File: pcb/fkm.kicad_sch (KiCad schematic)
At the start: 12 parts, among them U2 18650, U3 AMS1117-3.3

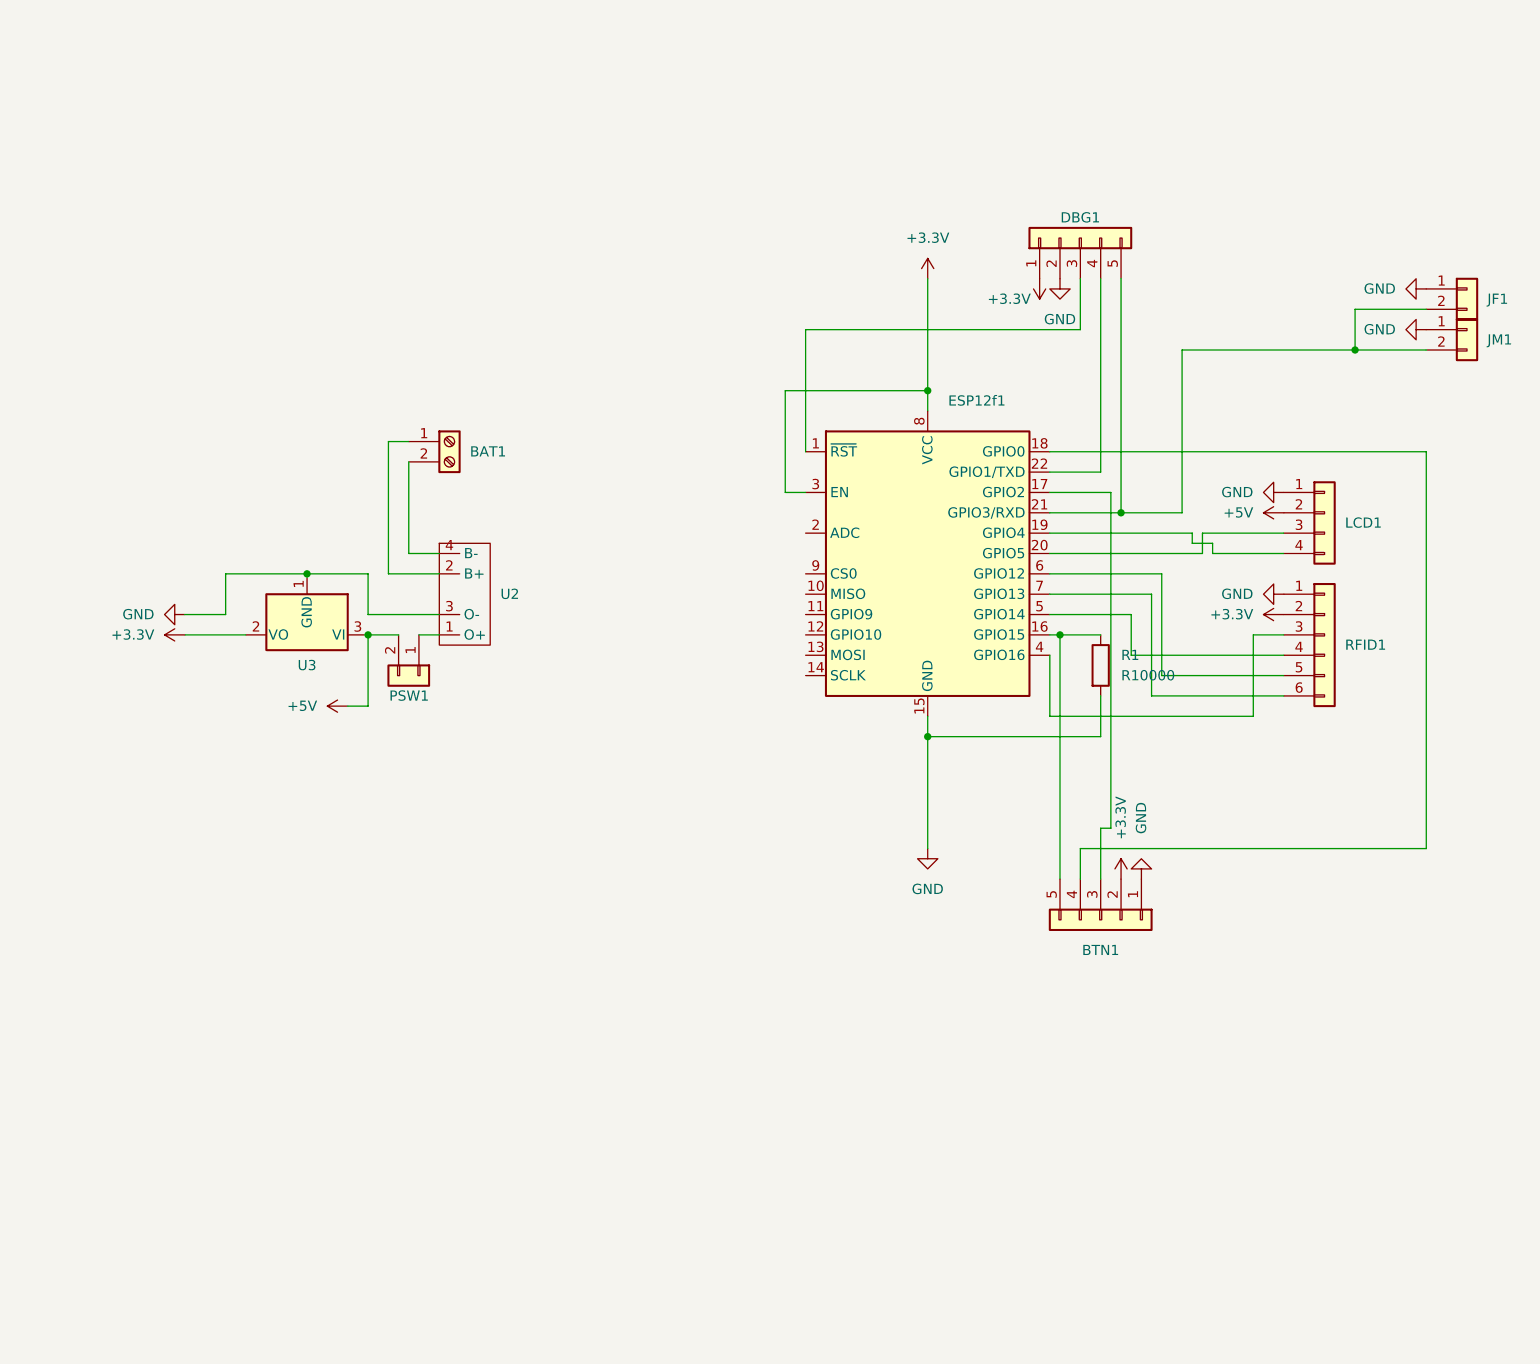
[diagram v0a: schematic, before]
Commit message: wip(pcb): rev 2.0 pcb (esp32) - to re-do
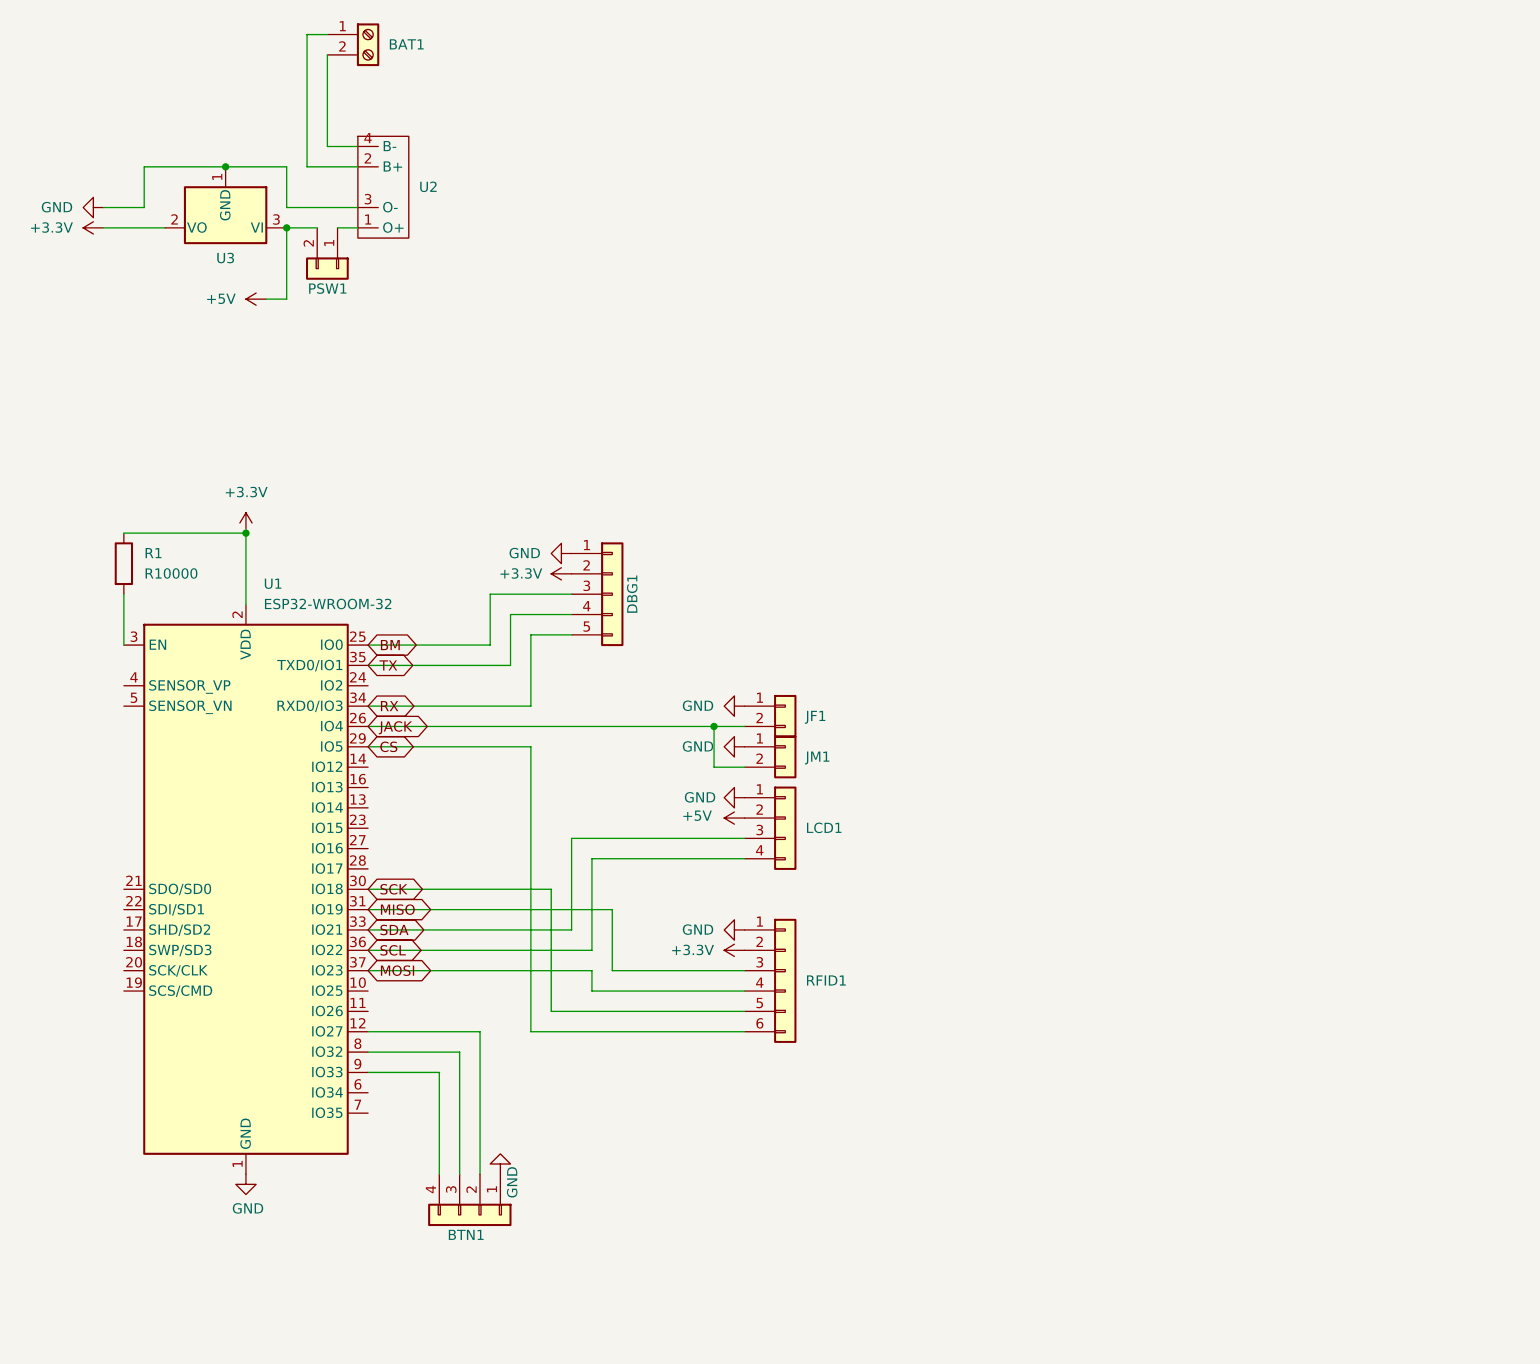
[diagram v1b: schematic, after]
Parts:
- removed BTN1: Conn_01x05, Connector_PinHeader_2.54mm:PinHeader_1x05_P2.54mm_Vertical, symbol Connector_Generic:Conn_01x05
- removed ESP12f1: ESP-12F/E, RF_Module:ESP-12E, symbol RF_Module:ESP-12F
- added BTN1: Conn_01x04, Connector_PinHeader_2.54mm:PinHeader_1x04_P2.54mm_Vertical, symbol Connector_Generic:Conn_01x04
- added U1: ESP32-WROOM-32, RF_Module:ESP32-WROOM-32, symbol RF_Module:ESP32-WROOM-32
- DBG1: footprint Connector_PinHeader_2.54mm:PinHeader_1x05_P2.54mm_Vertical -> Connector_PinHeader_2.00mm:PinHeader_1x05_P2.00mm_Vertical
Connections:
- net +3.3V: now also DBG1.2 (Pin_2), R1.1, U1.2 (VDD); no longer DBG1.1 (Pin_1)
- net GND: now also DBG1.1 (Pin_1), BTN1.1 (Pin_1), U1.1 (GND), U1.15 (GND), U1.38 (GND), U1.39 (GND); no longer DBG1.2 (Pin_2), R1.2
- net MISO: now reaches RFID1.3 (Pin_3)
- net MISO: now also U1.31 (IO19)
- net MOSI: now reaches RFID1.4 (Pin_4)
- net MOSI: now also U1.37 (IO23)
- net SCK: now reaches RFID1.5 (Pin_5)
- net SCK: now also U1.30 (IO18)
- net CS: now reaches RFID1.6 (Pin_6)
- net CS: now also U1.29 (IO5)
- net BM: now reaches DBG1.3 (Pin_3)
- net BM: now also U1.25 (IO0)
- net TX: now reaches DBG1.4 (Pin_4)
- net TX: now also U1.35 (TXD0/IO1)
- net JACK: now reaches JF1.2 (Pin_2), JM1.2 (Pin_2)
- net JACK: now also U1.26 (IO4); no longer DBG1.5 (Pin_5)
- net SCL: now reaches LCD1.4 (Pin_4)
- net SCL: now also U1.36 (IO22)
- net SDA: now reaches LCD1.3 (Pin_3)
- net SDA: now also U1.33 (IO21)
- new net: BTN1.2 (Pin_2), U1.12 (IO27)
- new net: R1.2, U1.3 (EN)
- new net: BTN1.3 (Pin_3), U1.8 (IO32)
- new net: BTN1.4 (Pin_4), U1.9 (IO33)
- new net RX: DBG1.5 (Pin_5), U1.34 (RXD0/IO3)
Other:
- moved on the sheet: BAT1, DBG1, JF1, JM1, LCD1, PSW1, R1, RFID1, U2, U3

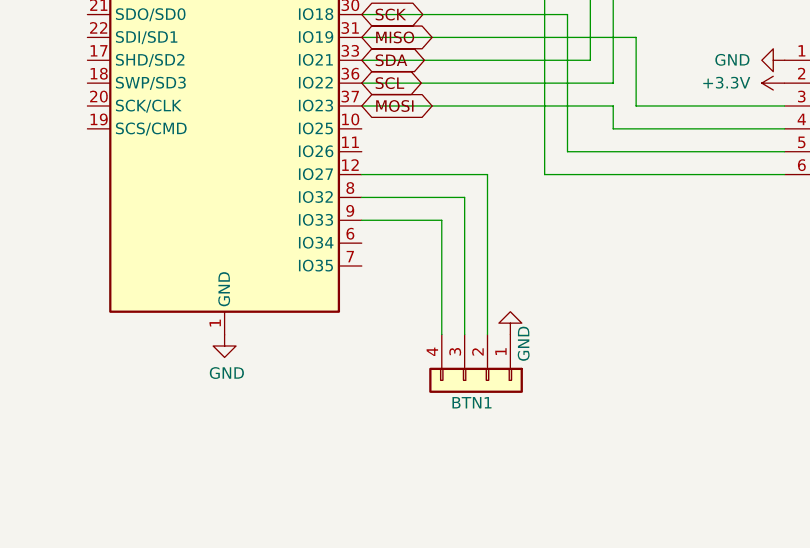
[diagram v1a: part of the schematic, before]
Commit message: feat(pcb): battery level input (ADC)
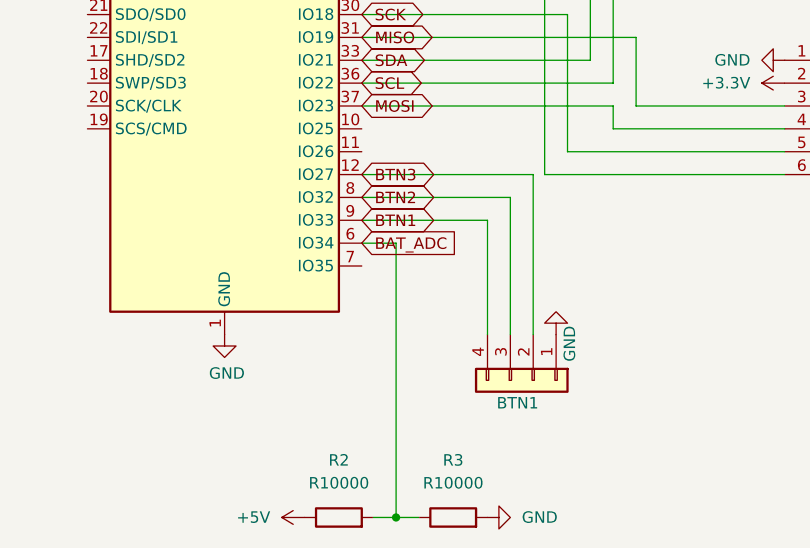
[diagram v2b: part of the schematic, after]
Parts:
- added R2, R3: R10000, Resistor_SMD:R_0805_2012Metric_Pad1.20x1.40mm_HandSolder, symbol Device:R
- R1: footprint Resistor_THT:R_Axial_DIN0204_L3.6mm_D1.6mm_P7.62mm_Horizontal -> Resistor_SMD:R_0805_2012Metric_Pad1.20x1.40mm_HandSolder
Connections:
- net +5V: now also R2.1
- net GND: now also R3.2
- net BTN3: now reaches BTN1.2 (Pin_2), U1.12 (IO27)
- net BAT_ADC: now reaches U1.6 (IO34)
- net BAT_ADC: now also R2.2, R3.1
- net BTN2: now reaches BTN1.3 (Pin_3), U1.8 (IO32)
- net BTN1: now reaches BTN1.4 (Pin_4), U1.9 (IO33)
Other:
- moved on the sheet: BTN1

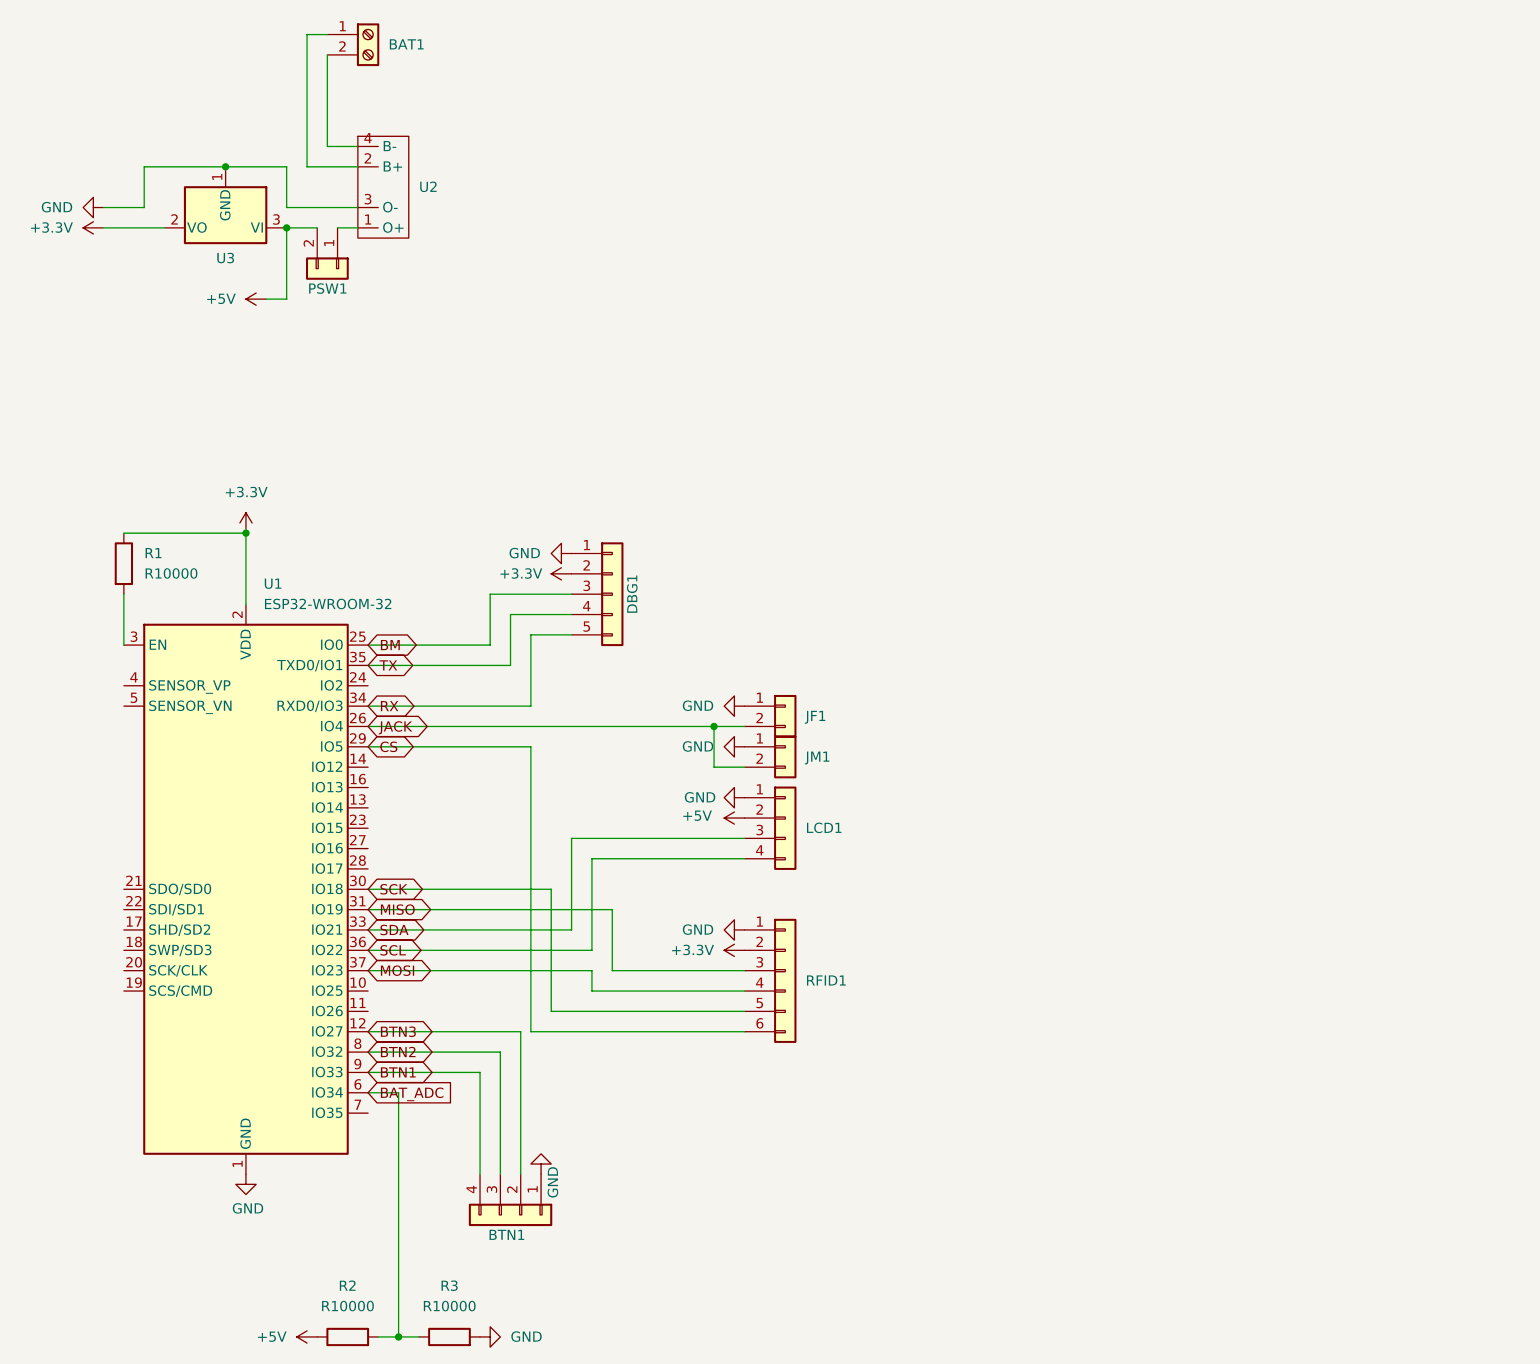
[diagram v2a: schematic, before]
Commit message: wip(pcb): re-wire everything (now its not messy)
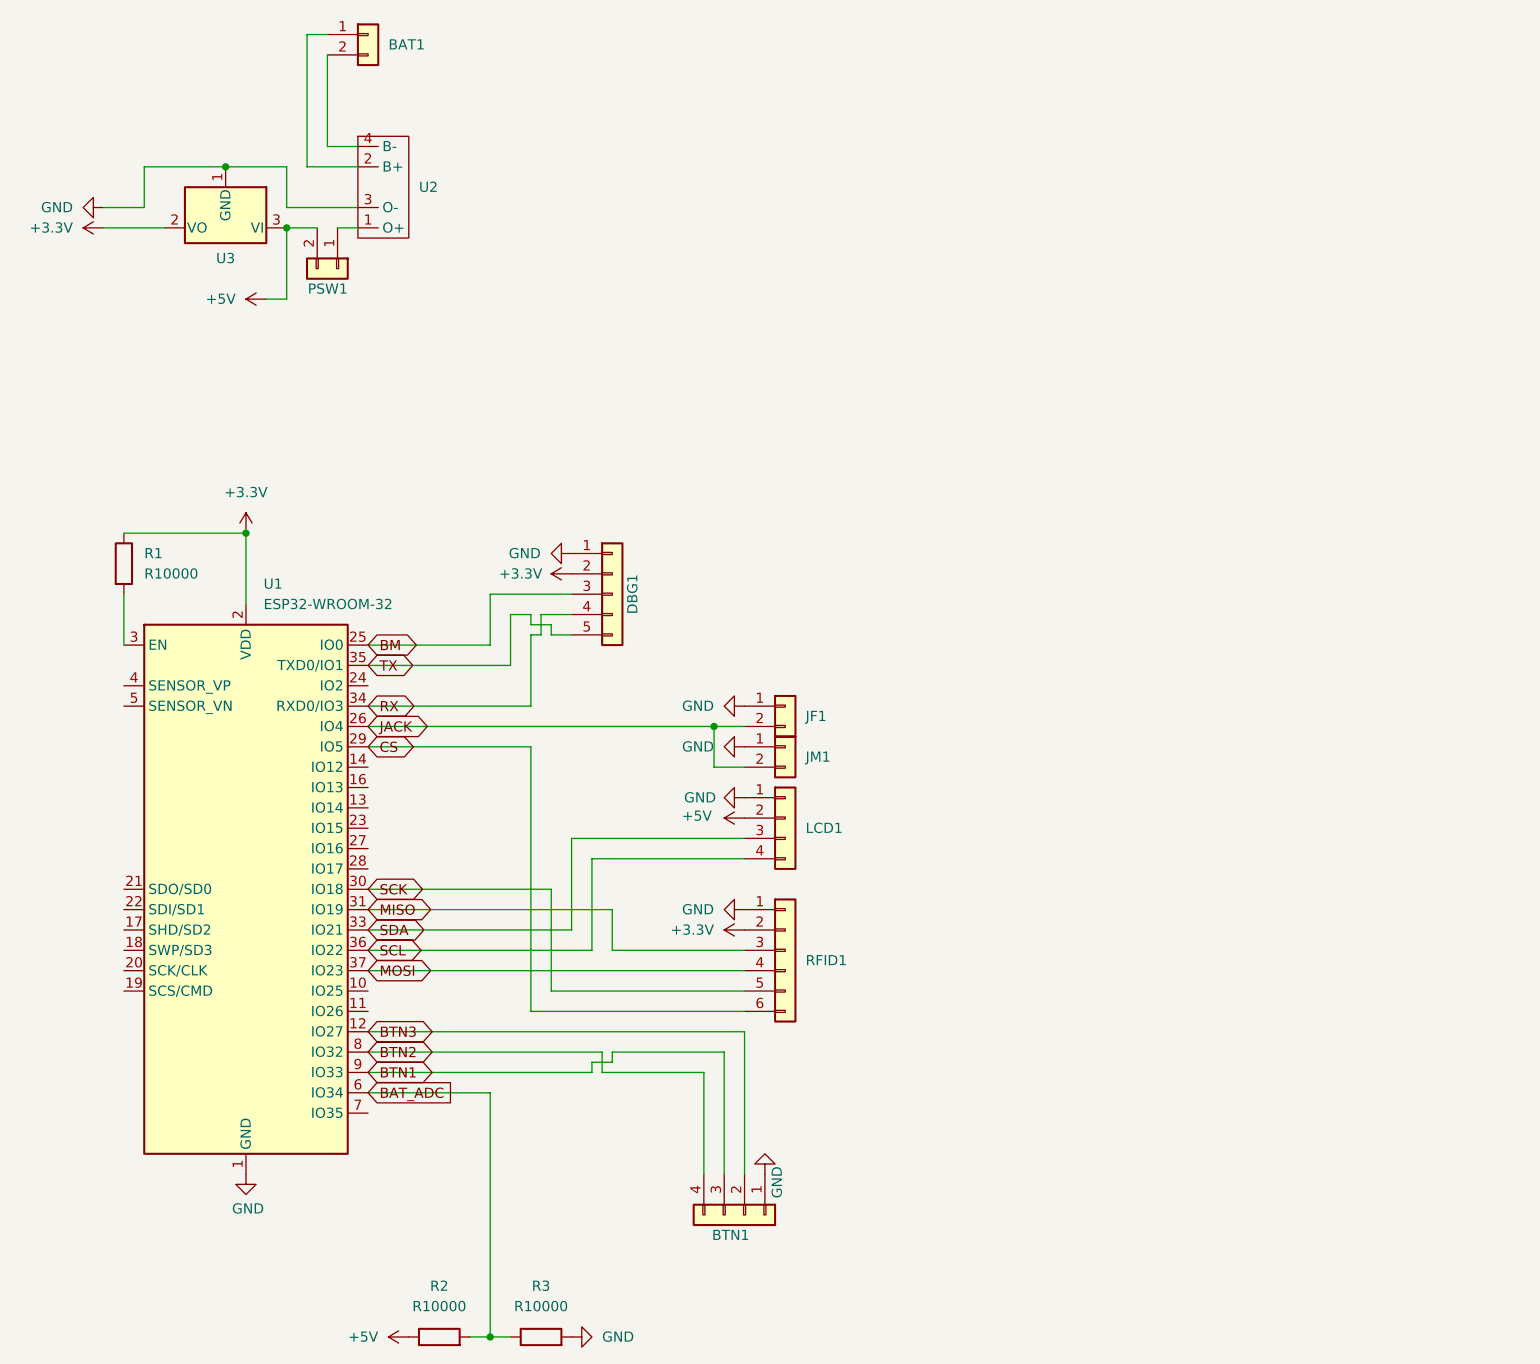
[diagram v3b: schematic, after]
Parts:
- removed BAT1: Screw_Terminal_01x02, TerminalBlock_4Ucon:TerminalBlock_4Ucon_1x02_P3.50mm_Horizontal, symbol Connector:Screw_Terminal_01x02
- added BAT1: BAT1, Connector_PinHeader_2.54mm:PinHeader_1x02_P2.54mm_Vertical, symbol Connector_Generic:Conn_01x02
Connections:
- net BTN1: now also BTN1.3 (Pin_3); no longer BTN1.4 (Pin_4)
- net BTN2: now also BTN1.4 (Pin_4); no longer BTN1.3 (Pin_3)
- net RX: now also DBG1.4 (Pin_4); no longer DBG1.5 (Pin_5)
- net TX: now also DBG1.5 (Pin_5); no longer DBG1.4 (Pin_4)
- net at U2.2 (B+): now also BAT1.1 (Pin_1)
- net at U2.4 (B-): now also BAT1.2 (Pin_2)
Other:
- moved on the sheet: BTN1, R2, R3, RFID1
